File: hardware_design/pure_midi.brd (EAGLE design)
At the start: 68.8 x 100 mm, 60 parts, among them IC1 74HC165D, IC2 VOLTAGE_REG_POS05DT, Q1 20MHz, T1 MMBT3904, T2 MMBT3904, T3 MMBT3904, T4 MMBT3904, U1 ANALOG_DEVICES_INC_AD5754AREZ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, U2 TEXAS_INSTRUMENTS_LM4040C25ID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, U3 ATMEGA328P_TQFP, X1 OG-MIDI_MAB5SHCUI-SD-50BV

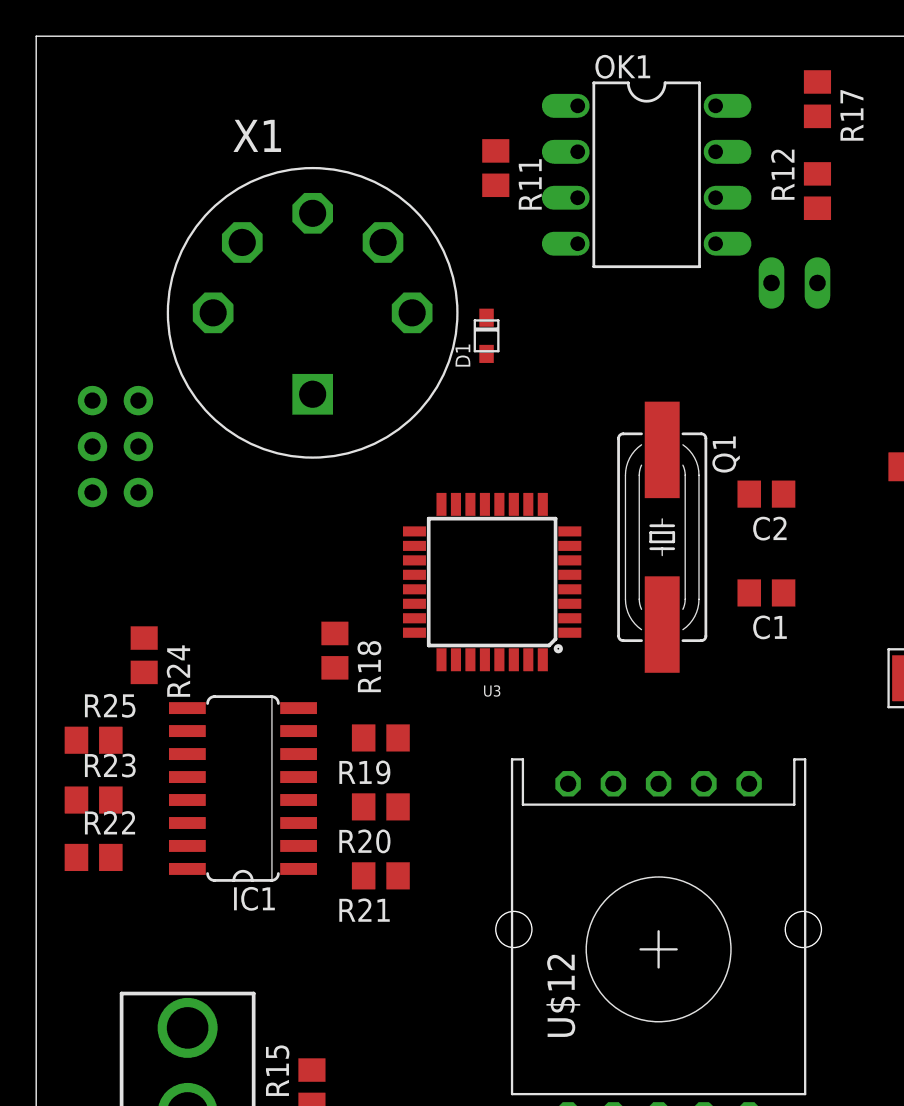
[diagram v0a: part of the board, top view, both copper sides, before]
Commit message: Use different one-hot to binary encoder
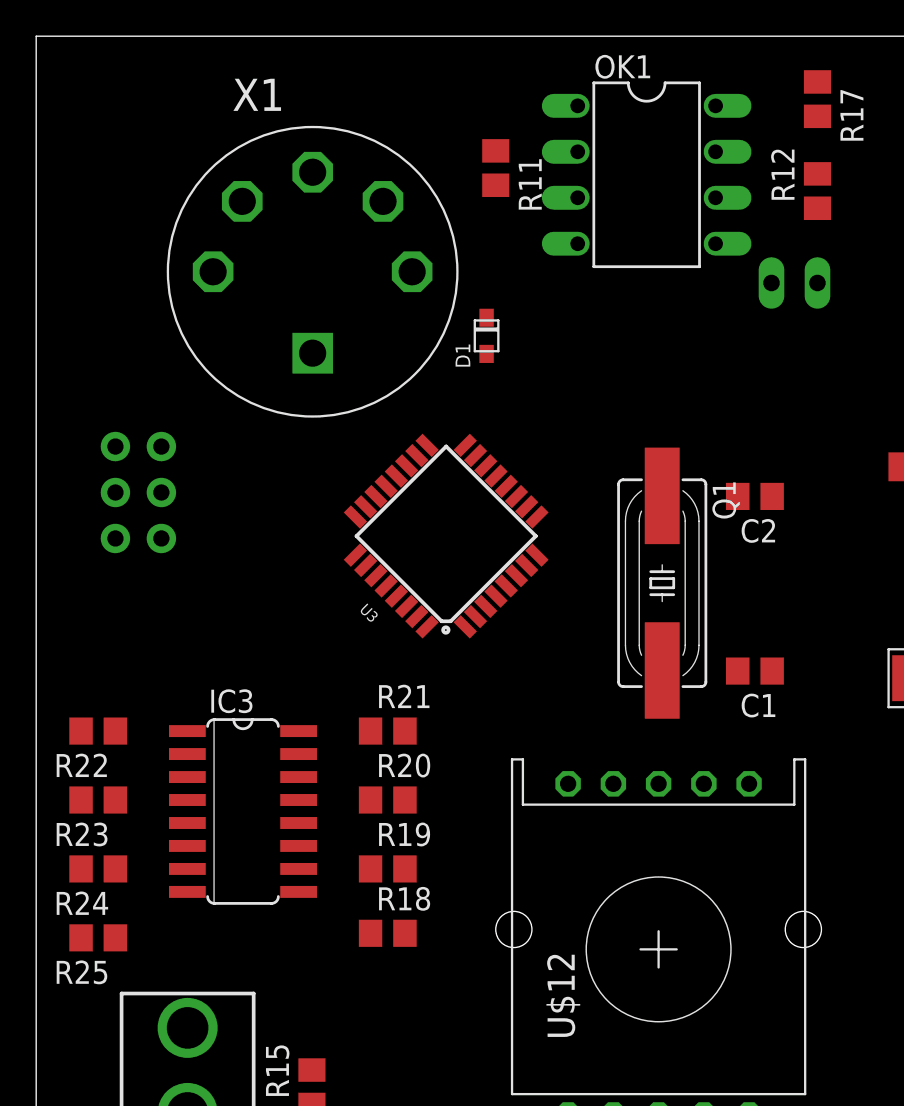
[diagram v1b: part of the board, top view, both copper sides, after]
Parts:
- removed IC1: 74HC165D, 74xx-eu:SO16
- added IC3: 74HC148D, 74xx-eu:SO16
- moved R18 15.9 mm to (19.4, 50.4), turned to 0 degrees
- moved R24 12.1 mm to (3.43, 54.0), turned to 180 degrees
- moved R25 10.9 mm to (3.43, 50.2), turned to 180 degrees
- moved R21 8.01 mm to (19.4, 61.6), turned to 0 degrees
- moved R19 7.25 mm to (19.4, 54.0), turned to 0 degrees
- moved R22 6.99 mm to (3.43, 61.6), turned to 180 degrees
- moved C1 4.36 mm to (39.7, 64.9)
- moved U3 3.59 mm to (22.7, 72.4), turned to 135 degrees
- moved ISP1 2.84 mm to (5.65, 74.8)
- moved Q1 2.54 mm to (34.6, 69.8)
- moved X1 2.27 mm to (15.3, 87.0)
- moved C2 0.65 mm to (39.7, 74.6)
- moved R20 0.54 mm to (19.4, 57.8), turned to 0 degrees
- moved R23 0.25 mm to (3.43, 57.8), turned to 180 degrees
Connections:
- removed net N$17: IC1.12, R24.2, U$12.B
- removed net N$18: IC1.13, R23.2, U$12.C
- removed net N$19: IC1.14, R22.2, U$12.D
- removed net N$21: IC1.3, R21.2, U$12.E
- removed net N$22: IC1.4, R20.2, U$12.F
- removed net N$23: IC1.5, R19.2, U$12.G
- removed net N$24: IC1.6, R18.2, U$12.H
- removed net ROTARY_CLK: IC1.2, U3.2
- removed net ROTARY_DAT: IC1.9, U3.32
- removed net ROTARY_LD: IC1.1, U3.1
- new net N$26: IC3.11, R19.1, U$12.B
- new net N$27: IC3.12, R20.1, U$12.C
- new net N$28: IC3.13, R21.1, U$12.D
- new net N$29: IC3.1, R22.1, U$12.E
- new net N$30: IC3.2, R23.1, U$12.F
- new net N$31: IC3.3, R24.1, U$12.G
- new net N$32: IC3.4, R25.1, U$12.H
- new net ROTARY_D0: IC3.9, U3.32
- new net ROTARY_D1: IC3.7, U3.1
- new net ROTARY_D2: IC3.6, U3.2
- net +5V: now also IC3.16, R18.2, R19.2, R20.2, R21.2, R22.2, R23.2, R24.2, R25.2; no longer IC1.16, U$12.COM, U$12.COM2
- net GND: now also IC3.5, IC3.8, U$12.COM, U$12.COM2; no longer IC1.15, IC1.8, R18.1, R19.1, R20.1, R21.1, R22.1, R23.1, R24.1, R25.1
- net N$15: now also IC3.10, R18.1; no longer IC1.11, R25.2

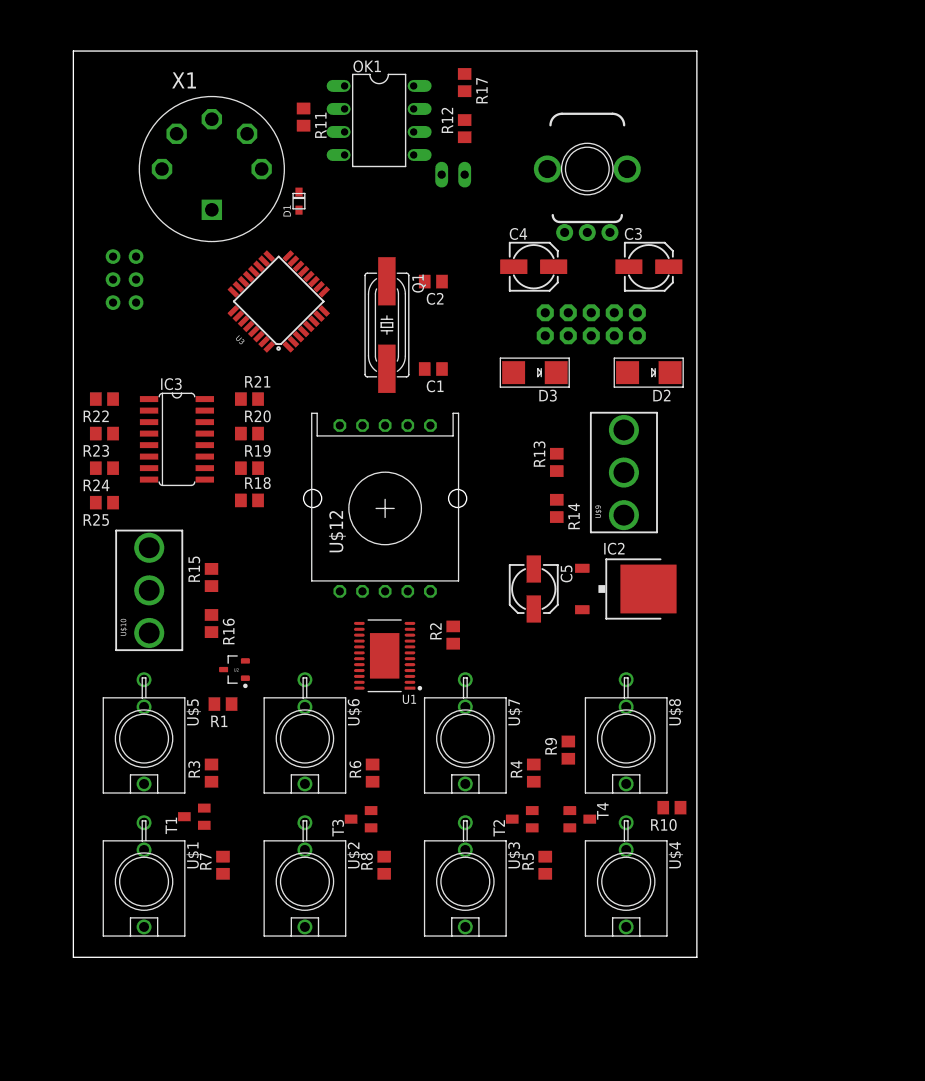
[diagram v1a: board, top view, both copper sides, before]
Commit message: Add USB Interface (completely untested)
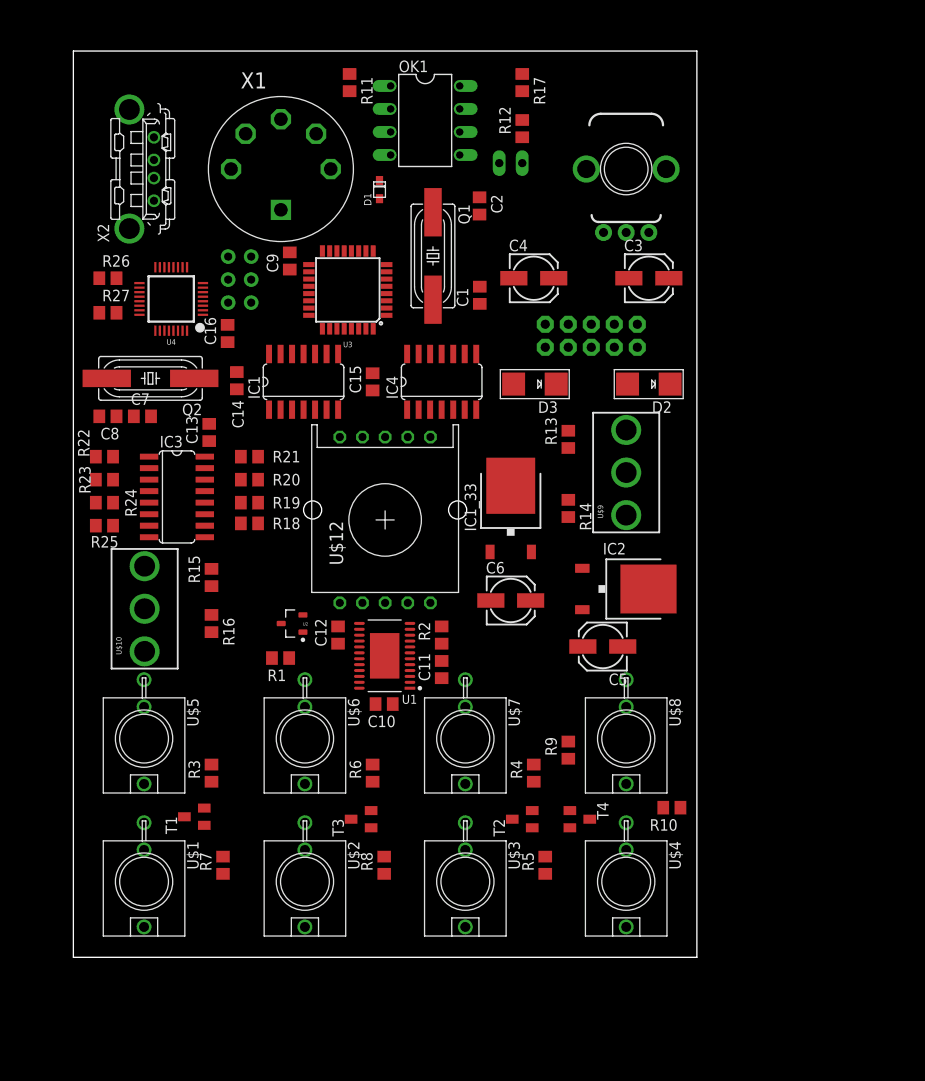
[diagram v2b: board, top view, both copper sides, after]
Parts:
- added C10, C11, C12, C13, C14, C15, C16, C9: 100n, rcl:C0805
- added C6: 47u, GMSN:153CLV-0505
- added C7, C8: 22p, rcl:C0805
- added IC1, IC4: 74HCT125D, 74xx-eu:SO14
- added IC1_33: VOLTAGE_REG_POSDT, GMSN:TO252
- added Q2: (no value), adafruit:HC49UP
- added R26, R27: 33R, rcl:R0805
- added U4: MAX3421, SparkFun-IC-Comms:TQFP32-5MM
- added X2: KUSBVX, con-kycon:KUSBVX
- C3, C4, C5: value (none) -> 47u
- moved ISP1 12.7 mm to (18.4, 74.8)
- moved C5 9.92 mm to (58.4, 34.3), turned to 180 degrees
- moved C2 9.77 mm to (44.8, 82.9), turned to 270 degrees
- moved C1 9.62 mm to (44.8, 73.1), turned to 90 degrees
- moved Q1 9.16 mm to (39.7, 77.4)
- moved D1 8.98 mm to (33.8, 84.7)
- moved R1 8.13 mm to (22.9, 33.0)
- moved U2 8.13 mm to (24.1, 36.8)
- moved U3 7.73 mm to (30.3, 73.6), turned to 180 degrees
- moved X1 7.62 mm to (22.9, 87.0)
- moved JP1 6.48 mm to (48.3, 87.6), turned to 90 degrees
- moved R11 6.35 mm to (30.5, 96.5)
- moved IC3 6.35 mm to (11.4, 50.8)
- moved R12 6.35 mm to (49.5, 91.4)
- moved R17 6.35 mm to (49.5, 96.5)
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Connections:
- net SS renamed SS_DAC
- new net +3V3: C14.1, C16.1, C6.+, IC1.14, IC1_33.2, U4.2, U4.23
- new net INT_USB: IC4.6, U3.13
- new net INT_USB_3V3: IC4.5, U4.18
- new net MISO_3V3: IC4.2, U4.15
- new net MOSI_3V3: IC1.8, U4.16
- new net N$19: C8.2, Q2.2, U4.25
- new net N$25: C7.2, Q2.1, U4.24
- new net RES_USB_3V3: U4.12
- new net RST_USB: IC1.12, U3.11
- new net RST_USB_3V3: IC1.11
- new net SCK_3V3: IC1.3, U4.13
- new net SS_USB: IC1.5, IC4.1, U3.12
- new net SS_USB_3V3: IC1.6, U4.14
- new net USB_D_N: R26.1, X2.2
- new net USB_D_P: R27.1, X2.3
- new net USB_N: R26.2, U4.20
- new net USB_P: R27.2, U4.21
- new net USB_VBUS: X2.1
- net +12V: now also C11.1, IC1_33.1
- net +5V: now also C12.1, C13.1, C15.1, C9.1, IC4.14
- net -12V: now also C10.2
- net GND: now also C10.1, C11.2, C12.2, C13.2, C14.2, C15.2, C16.2, C6.-, C7.1, C8.1, C9.2, IC1.1, IC1.10, IC1.13, IC1.4, IC1.7, IC1_33.3, IC4.4, IC4.7, U4.19, U4.3, X2.4, X2.M1, X2.M2
- net MISO: now also IC4.3
- net MOSI: now also IC1.9
- net SCK: now also IC1.2

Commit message: Specify USB Host Clock Frequency
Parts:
- Q2: value (none) -> 12MHz
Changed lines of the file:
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@@
 <attribute name="NAME" x="45.52" y="42.35" size="1.27" layer="25"/>
 </element>
-<element name="Q2" library="adafruit" library_urn="urn:adsk.eagle:library:420" package="HC49UP" package3d_urn="urn:adsk.eagle:package:6240908/1" value="" x="8.509" y="63.881" smashed="yes" rot="R180">
+<element name="Q2" library="adafruit" library_urn="urn:adsk.eagle:library:420" package="HC49UP" package3d_urn="urn:adsk.eagle:package:6240908/1" value="12MHz" x="8.509" y="63.881" smashed="yes" rot="R180">
 <attribute name="MF" value="" x="8.509" y="63.881" size="1.778" layer="27" rot="R180" display="off"/>
 <attribute name="MPN" value="" x="8.509" y="63.881" size="1.778" layer="27" rot="R180" display="off"/>

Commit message: First Revision
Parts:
- moved R10 13.1 mm to (54.6, 10.2), turned to 90 degrees
- moved C11 12.7 mm to (27.9, 31.8)
- moved C8 6.35 mm to (10.2, 59.7), turned to 0 degrees
- moved C7 3.81 mm to (3.81, 59.7)
- moved R9 2.54 mm to (54.6, 20.3)
- moved R5 1.27 mm to (50.8, 10.2)
- moved R7 1.27 mm to (15.2, 10.2)
- moved C12 1.27 mm to (27.9, 35.6)
- moved R8 1.27 mm to (33.0, 10.2)
- moved D1 0.90 mm to (33.9, 85.6), turned to 0 degrees
- moved C13 0.57 mm to (14.5, 58.2), turned to 180 degrees
- moved R2 0.25 mm to (40.9, 35.6)
- moved C10 0.13 mm to (34.2, 27.9), turned to 0 degrees
- turned Q2 to 0 degrees
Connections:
- removed net AGND: T1.E, T2.E, T3.E, T4.E, U$1.P$3, U$2.P$3, U$3.P$3, U$4.P$3, U$5.P$3, U$6.P$3, U$7.P$3, U$8.P$3, U1.18, U1.19, U1.20, U1.21, U2.2, U3.21
- removed net RES_USB_3V3: U4.12
- removed net USB_VBUS: X2.1
- net +5V: now also X2.1
- net GND: now also T1.E, T2.E, T3.E, T4.E, U$1.P$3, U$2.P$3, U$3.P$3, U$4.P$3, U$5.P$3, U$6.P$3, U$7.P$3, U$8.P$3, U1.18, U1.19, U1.20, U1.21, U2.2, U3.21
- net RST_USB_3V3: now also U4.12
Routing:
- net +5V: track 0.00 -> 314.9 mm, vias 0 -> 2
- net GND: track 0.00 -> 245.0 mm, vias 0 -> 68
- net +12V: track 0.00 -> 212.4 mm
- net D_GATE_OUT_3: track 0.00 -> 115.7 mm, vias 0 -> 2
- net SWITCH0_VAL: track 0.00 -> 96.5 mm, vias 0 -> 6
- net N$32: track 0.00 -> 91.7 mm
- net D_GATE_OUT_1: track 0.00 -> 89.5 mm, vias 0 -> 2
- net MOSI: track 0.00 -> 82.5 mm, vias 0 -> 3
- net +3V3: track 0.00 -> 78.9 mm, vias 0 -> 4
- net CV_OUT_1: track 0.00 -> 76.4 mm, vias 0 -> 2
- net D_GATE_OUT_4: track 0.00 -> 75.7 mm, vias 0 -> 2
- net SCK: track 0.00 -> 75.4 mm, vias 0 -> 3
- net N$30: track 0.00 -> 73.1 mm, vias 0 -> 2
- net SWITCH1_VAL: track 0.00 -> 68.9 mm, vias 0 -> 3
- net D_GATE_OUT_2: track 0.00 -> 66.4 mm, vias 0 -> 2
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- added copper zone on layer 1, net GND
- added copper zone on layer 16, net GND
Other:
- board text added: "Pure MIDI v0.1"
- board text added: "jhbruhn 2018"

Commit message: Rev 1/2
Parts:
- removed IC1_33: VOLTAGE_REG_POSDT, GMSN:TO252
- removed ISP1: AVRISP-6, adafruit:AVRISP
- removed JP1: (no value), jumper:JP1
- removed OK1: 6N138, optocoupler:DIL08
- removed Q1: 20MHz, adafruit:HC49UP
- removed Q2: 12MHz, adafruit:HC49UP
- removed R22, R23, R24, R25: 10k, rcl:R0805
- removed T1, T2, T3, T4: MMBT3904, transistor:SOT23-EBC
- removed U$10, U$9: TOGGLE_ON_OFF_ON, INSTRUO:TOGGLE_ON_OFF_ON
- added C17, C21, C23, C24, C25, C26: 100n, rcl:C0603
- added DI1: OLED_1.3_128X64_SPI, microbuilder:C1_ADAFRUIT_1.3_128X64_OLED
- added FD1, FD2, FD3, FD4: FIDUCIALUFIDUCIAL, SparkFun-Aesthetics:FIDUCIAL-MICRO
- added IC5: STM32F10XCXT6, stm32:TQFP48
- added IC6: LD117AS33TR, v-reg:SOT223
- added J1: CORTEX_DEBUG_PTH, SparkFun-Connectors:2X5-PTH-1.27MM
- added LOGO1: OSHW-LOGOM, SparkFun-Aesthetics:OSHW-LOGO-M
- added SW1: EC12E_SW, switch-alps:ALPS_EC12E_SW
- added U$13, U$14, U$15, U$16, U$17, U$18, U$19, U$20: WQP-PJ301M-12_JACK, thonkiconn:WQP-PJ301M-12_JACK
- added U5: TEXAS_INSTRUMENTS_LM4040C25IDBZRTEXAS_INSTRUMENTS_LM4040C25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, lm4040:TEXAS_INSTRUMENTS_LM4040C25IDBZR_1
- added X3: OG-MIDI_MAB5SHCUI-SD-50BV, yarns_v03:OG-MIDI_SD-50BV
- added X4: KUSBVX-BS1N, con-kycon:KUSBVX-BS1N
- added X6: ABRACON_ABM3B-12.000MHZ-B2-TABRACON_ABM3B-12.000MHZ-B2-T_0_0, Abracon - ABM3B-12.000MHZ-B2-T:ABRACON_ABM3B-12.000MHZ-B2-T_0
- added X7: ABRACON_ABM3B-8.000MHZ-B2-TABRACON_ABM3B-8.000MHZ-B2-T_0_0, Abracon - ABM3B-8.000MHZ-B2-T:ABRACON_ABM3B-8.000MHZ-B2-T_0
- C1, C10, C11, C12, C13, C14, C15, C16, C2, C7, C8, C9: device rcl:C0805 -> rcl:C0603
- C3, C4, C5, C6: value 47u -> 22u
- IC1: value 74HCT125D -> LD117AS50TR; device 74xx-eu:SO14 -> v-reg:SOT223
- IC2: value VOLTAGE_REG_POS05DT -> 74HCT125D; device GMSN:TO252 -> 74xx-eu:SO14
- IC3: value 74HC148D -> 6N138SMD; device 74xx-eu:SO16 -> 6n138:SO8-GW300
- R1: value 2k -> 1k; device rcl:R0805 -> rcl:R0603
- R10, R9: value 1k -> 51R; device rcl:R0805 -> rcl:R0603
- R11, R12, R17: device resistor:R0805 -> rcl:R0603
- R13, R14: value 10k -> 22R; device resistor:R0805 -> rcl:R0603
- R15, R16: device resistor:R0805 -> resistor:R0603
- R18, R19: value 10k -> 2k; device rcl:R0805 -> rcl:R0603
- R2, R21, R26, R27, R4, R5, R6, R7, R8: device rcl:R0805 -> rcl:R0603
- R20: value 10k -> 1k5; device rcl:R0805 -> rcl:R0603
- R3: value 1k -> 4k7; device rcl:R0805 -> rcl:R0603
- U$11: value Q-POT -> WQP-PJ301M-12_JACK; device INSTRUO:Q-POT -> thonkiconn:WQP-PJ301M-12_JACK
- U$12: value ALPS-SRBV -> WQP-PJ301M-12_JACK; device TomW:ALPS-SRBV -> thonkiconn:WQP-PJ301M-12_JACK
- U1: value ANALOG_DEVICES_INC_AD5754AREZANALOG_DEVICES_INC_AD5754AREZ_0_0 -> AD5676ARUZ; device Analog Devices Inc - AD5754AREZ:ANALOG_DEVICES_INC_AD5754AREZ_0 -> AD5676ARUZ:RU_20
- U2: value TEXAS_INSTRUMENTS_LM4040C25IDBZRTEXAS_INSTRUMENTS_LM4040C25IDBZR_0_1 -> AD5754BREZ; device Texas Instruments - LM4040C25IDBZR:TEXAS_INSTRUMENTS_LM4040C25IDBZR_1 -> ad5754:RE_24
- U3: value ATMEGA328P_TQFP -> TEXAS_INSTRUMENTS_LM4040C5IDBZR1; device SparkFun-IC-Microcontroller:TQFP32-08 -> lm4040:TEXAS_INSTRUMENTS_LM4040C5IDBZR_1
- moved R7 90.1 mm to (69.1, 82.4), flipped to the bottom, turned to 0 degrees
- moved X1 78.8 mm to (8.68, 9.53)
- moved U$11 69.9 mm to (39.1, 20.6), turned to 180 degrees
- moved R8 68.4 mm to (68.6, 68.6), flipped to the bottom, turned to 0 degrees
- moved C10 62.5 mm to (33.0, 90.4), flipped to the bottom, turned to 180 degrees
- moved R17 58.5 mm to (2.29, 62.0), flipped to the bottom
- moved X2 58.2 mm to (7.37, 28.8), turned to 270 degrees
- moved R12 57.6 mm to (2.29, 58.4), flipped to the bottom
- moved R16 57.2 mm to (53.5, 79.4), flipped to the bottom, turned to 90 degrees
- moved IC1 56.9 mm to (72.9, 94.8), flipped to the bottom, turned to 90 degrees
- moved C5 55.6 mm to (74.2, 87.6), flipped to the bottom, turned to 0 degrees
- moved C6 51.3 mm to (65.5, 87.6), flipped to the bottom
- moved IC2 51.0 mm to (32.9, 83.2), flipped to the bottom
- moved R15 50.4 mm to (48.9, 79.4), flipped to the bottom
- moved R26 47.2 mm to (3.81, 27.7), flipped to the bottom
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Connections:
- removed net AREF: R1.1, U1.17, U2.1
- removed net INT_USB_3V3: IC4.5, U4.18
- removed net MISO_3V3: IC4.2, U4.15
- removed net MOSI_3V3: IC1.8, U4.16
- removed net N$16: R14.2, U$9.1
- removed net N$25: C7.2, Q2.1, U4.24
- removed net N$26: IC3.11, R19.1, U$12.B
- removed net N$27: IC3.12, R20.1, U$12.C
- removed net N$28: IC3.13, R21.1, U$12.D
- removed net N$29: IC3.1, R22.1, U$12.E
- removed net N$30: IC3.2, R23.1, U$12.F
- removed net N$31: IC3.3, R24.1, U$12.G
- removed net N$32: IC3.4, R25.1, U$12.H
- removed net ROTARY_D0: IC3.9, U3.32
- removed net ROTARY_D1: IC3.7, U3.1
- removed net ROTARY_D2: IC3.6, U3.2
- removed net RST_USB_3V3: IC1.11, U4.12
- removed net SCK_3V3: IC1.3, U4.13
- removed net SPEED_VAL: U$11.P$2, U3.27
- removed net SS_DAC: U1.7, U3.14
- removed net SS_USB_3V3: IC1.6, U4.14
- removed net SWITCH0_VAL: R13.1, U$9.2, U3.19
- removed net SWITCH1_VAL: R15.1, U$10.2, U3.22
- new net AREF_25: R18.1, U2.17, U5.1
- new net AREF_5: R19.1, U1.18, U3.1
- new net CV_OUT_10: U$16.P$1, U1.11
- new net CV_OUT_11: U$17.P$1, U1.10
- new net CV_OUT_12: U$18.P$1, U1.9
- new net CV_OUT_5: U$11.P$1, U1.2
- new net CV_OUT_6: U$12.P$1, U1.1
- new net CV_OUT_7: U$13.P$1, U1.20
- new net CV_OUT_8: U$14.P$1, U1.19
- new net CV_OUT_9: U$15.P$1, U1.12
- new net D_GATE_OUT_5: IC4.9, IC5.14
- new net D_GATE_OUT_6: IC4.12, IC5.15
- new net ENC_A: IC5.2, R15.1, SW1.A
- new net ENC_B: IC5.3, R16.1, SW1.B
- new net ENC_SW: IC5.4, SW1.E
- new net GATE_OUT_5: R7.1, U$19.P$1
- new net GATE_OUT_6: R8.1, U$20.P$1
- new net JTCK: IC5.37, J1.4
- new net JTDI: IC5.38, J1.8
- new net JTDO: IC5.39, J1.6
- new net JTMS: IC5.34, J1.2
- new net MIDI_DATA_OUT: IC5.30, R9.1
- new net N$17: IC4.8, R7.2
- new net N$18: IC4.11, R8.2
- new net N$21: R13.1, X4.2
- new net N$22: R10.1, X3.4
- new net N$23: R14.1, R20.2, X4.3
- new net SDC_OLED: DI1.SDC, IC5.25
- new net SS_DAC0: IC5.42, U1.5
- new net SS_DAC1: IC5.43, U2.7
- new net SS_OLED: DI1.CCS, IC5.22
- new net USB_PER_D_N: IC5.32, R13.2
- new net USB_PER_D_P: IC5.33, R14.2
- net +12V: now also C13.1, IC1.3, IC6.3, R18.2, R19.2, U1.3, U2.24; no longer IC1_33.1, IC2.1, R1.2, R10.1, R5.1, R7.1, R8.1, U1.24
- net +3V3: now also C15.1, C21.1, C23.1, C24.1, C25.1, IC3.8, IC5.1, IC5.24, IC5.36, IC5.48, IC5.9, IC6.4, J1.1, R10.2, R12.2, R20.1, R21.2; no longer IC1.14, IC1_33.2
- net +5V: now also C10.1, C17.1, DI1.VIN, IC1.4, IC2.14, R16.2, R3.2, U1.4, U2.14; no longer C13.1, C15.1, IC2.2, IC3.16, ISP1.2, OK1.8, R12.2, R13.2, R18.2, R19.2, R20.2, R21.2, R22.2, R23.2, R24.2, R25.2, U$11.P$3, U1.14, U3.18, U3.4, U3.6
- net -12V: now also C26.2, U2.1, U2.25; no longer C10.2, U1.1, U1.25
- net CV_OUT_1: now also U2.3; no longer U1.3
- net CV_OUT_2: now also U2.4; no longer U1.4
- net CV_OUT_3: now also U2.23; no longer U1.23
- net CV_OUT_4: now also U2.22; no longer U1.22
- net D_GATE_OUT_1: now also IC2.2, IC5.10; no longer R3.2, U3.28
- net D_GATE_OUT_2: now also IC2.5, IC5.11; no longer R6.2, U3.24
- net D_GATE_OUT_3: now also IC2.9, IC5.12; no longer R4.2, U3.25
- net D_GATE_OUT_4: now also IC2.12, IC5.13; no longer R9.2, U3.26
- net GATE_OUT_1: now also R1.1; no longer R7.2, T1.C
- net GATE_OUT_2: now also R4.1; no longer R8.2, T3.C
- net GATE_OUT_3: now also R5.1; no longer R5.2, T2.C
- net GATE_OUT_4: now also R6.1; no longer R10.2, T4.C
- net GND: now also C10.2, C17.2, C21.2, C23.2, C24.2, C25.2, C26.1, DI1.GND, IC2.1, IC2.10, IC2.13, IC2.4, IC2.7, IC4.10, IC4.13, IC5.20, IC5.23, IC5.35, IC5.44, IC5.47, IC5.8, IC6.1, J1.3, J1.5, J1.9, SW1.C, SW1.D, U$11.P$3, U$12.P$3, U$13.P$3, U$14.P$3, U$15.P$3, U$16.P$3, U$17.P$3, U$18.P$3, U$19.P$3, U$20.P$3, U1.13, U1.14, U2.10, U2.15, U2.18, U2.19, U2.20, U2.21, U2.5, U3.2, U5.2, X3.2, X4.4, X4.M1, X4.M2, X6.2, X6.4, X7.2, X7.4; no longer C10.1, IC1.10, IC1.13, IC1.4, IC1.7, IC1_33.3, IC2.3, IC3.8, IC4.4, ISP1.6, OK1.5, R14.1, R16.1, T1.E, T2.E, T3.E, T4.E, U$10.3, U$11.P$1, U$12.COM, U$12.COM2, U$9.3, U1.10, U1.18, U1.19, U1.20, U1.21, U1.5, U2.2, U3.21, U3.3, U3.5
- net INT_USB: now also IC5.21, U4.18; no longer IC4.6, U3.13
- net MIDI_DATA_IN: now also IC3.6, IC5.31; no longer JP1.2, OK1.6
- net MISO: now also IC5.27, U4.15; no longer IC4.3, ISP1.1, U3.16
- net MOSI: now also DI1.MOSI, IC5.28, U1.7, U2.9, U4.16; no longer IC1.9, ISP1.4, U1.9, U3.15
- net N$1: now also U1.8; no longer U1.11
- net N$10: now also IC2.3, R1.2; no longer JP1.1, U3.30
- net N$11: now also IC2.6, R4.2; no longer R9.1, T4.B
- net N$12: now also IC3.7; no longer OK1.7
- net N$14: now also IC2.8, R5.2; no longer R16.2, U$10.1
- net N$15: now also IC2.11, R6.2; no longer IC3.10, R18.1, U$12.A
- net N$19: now also R9.2, X3.5; no longer C8.2, Q2.2, U4.25
- net N$2: now also U2.11; no longer T1.B
- net N$3: now also C2.2, IC5.6, X7.3; no longer R4.1, T2.B
- net N$4: now also IC3.2; no longer OK1.2
- net N$6: now also IC5.5, X7.1; no longer Q1.2, U3.7
- net N$7: now also C8.2, U4.25, X6.1; no longer C2.2, Q1.1, U3.8
- net N$8: now also C7.2, U4.24, X6.3; no longer R6.1, T3.B
- net N$9: now also IC3.3; no longer OK1.3
- net RST: now also DI1.RES, IC5.7, J1.10, R21.1, U1.17; no longer ISP1.5, U3.29
- net RST_USB: now also IC5.45, U4.12; no longer IC1.12, U3.11
- net SCK: now also DI1.CLK, IC5.26, U1.6, U2.8, U4.13; no longer IC1.2, ISP1.3, U1.8, U3.17
- net SS_USB: now also IC5.46, U4.14; no longer IC1.5, IC4.1, U3.12
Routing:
- net GND: track 245.0 -> 738.1 mm, vias 68 -> 19
- net +3V3: track 78.9 -> 223.1 mm, vias 4 -> 32
- net +5V: track 314.9 -> 207.4 mm, vias 2 -> 27
- net CV_OUT_7: track 0.00 -> 107.2 mm, vias 0 -> 1
- net SWITCH0_VAL: track 96.5 -> 0.00 mm, vias 6 -> 0
- net MIDI_DATA_OUT: track 0.00 -> 93.6 mm, vias 0 -> 2
- net +12V: track 212.4 -> 118.8 mm, vias 0 -> 6
- net N$32: track 91.7 -> 0.00 mm
- net USB_PER_D_P: track 0.00 -> 86.7 mm
- net D_GATE_OUT_3: track 115.7 -> 33.9 mm
- net USB_PER_D_N: track 0.00 -> 77.9 mm
- net CV_OUT_12: track 0.00 -> 73.5 mm, vias 0 -> 2
- net N$30: track 73.1 -> 0.00 mm, vias 2 -> 0
- net CV_OUT_8: track 0.00 -> 70.1 mm, vias 0 -> 2
- net SWITCH1_VAL: track 68.9 -> 0.00 mm, vias 3 -> 0
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- added copper zone on layer 1, net +3V3
- added copper zone on layer 16, net +3V3
- added copper zone on layer 1, net +5V
- added copper zone on layer 16, net +5V
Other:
- board size 68.8 x 100 mm -> 78.9 x 100 mm
- board text added: "Pure MIDI v1"
- board text added: "ehre"
- board text added: "go vegan"
- board text added: "jhbruhn 2019"
- board text added: "peda b"
- board text removed: "Pure MIDI v0.1"
- board text removed: "jhbruhn 2018"
